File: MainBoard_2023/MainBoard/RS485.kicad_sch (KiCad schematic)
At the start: 18 parts

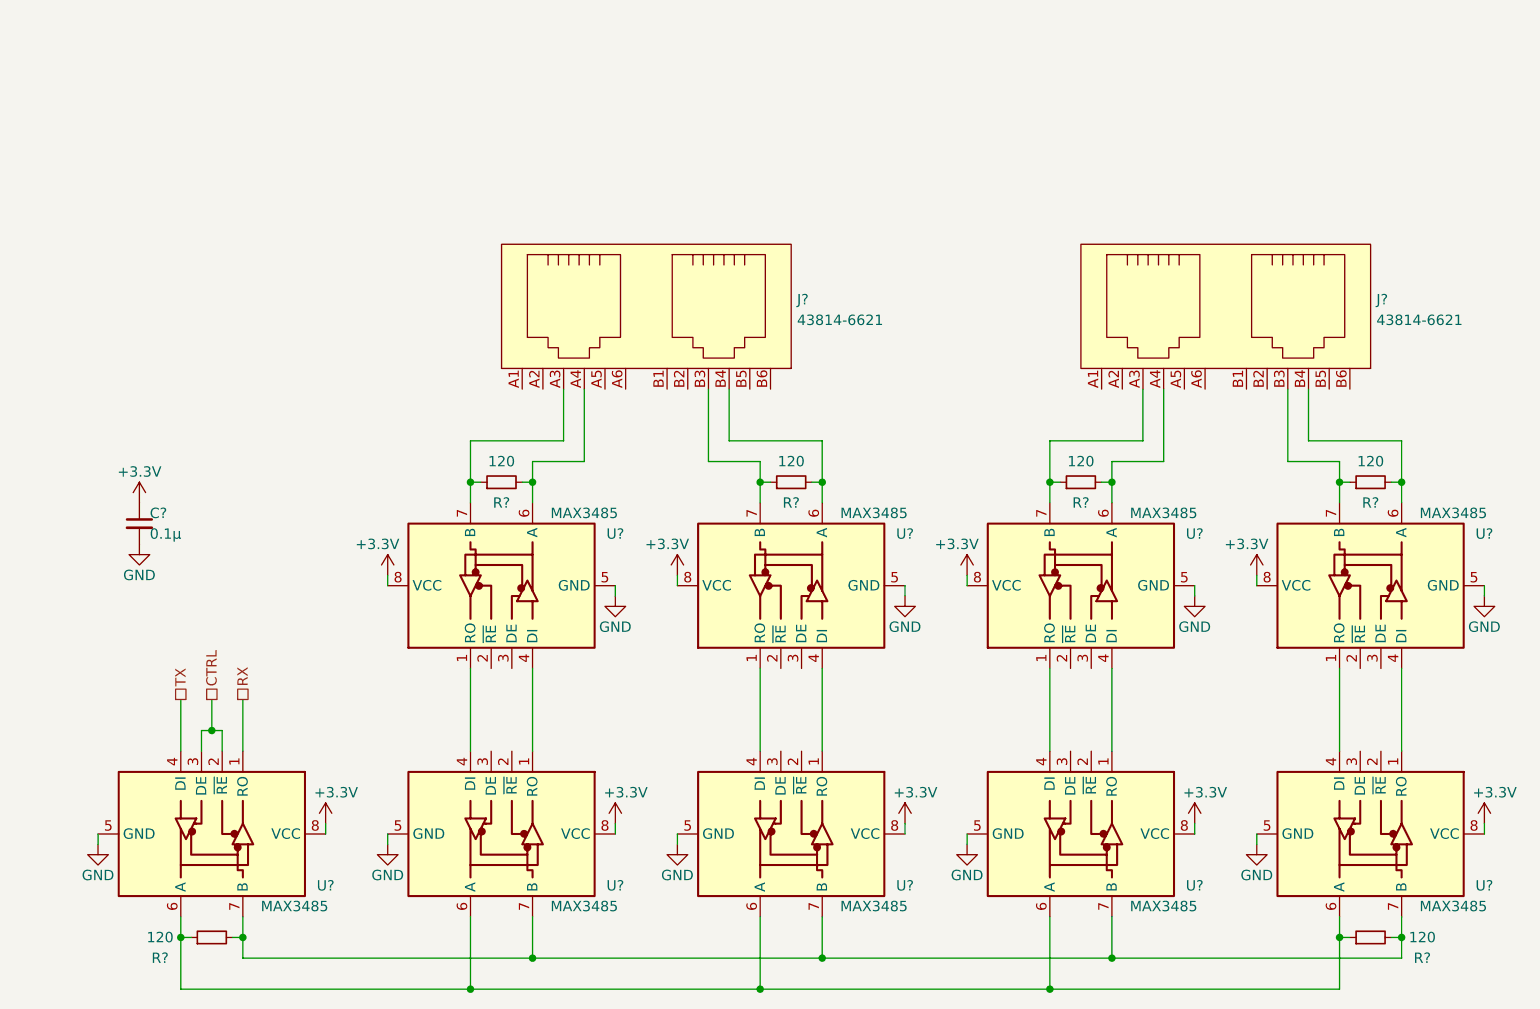
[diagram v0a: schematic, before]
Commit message: picoのピンを設定
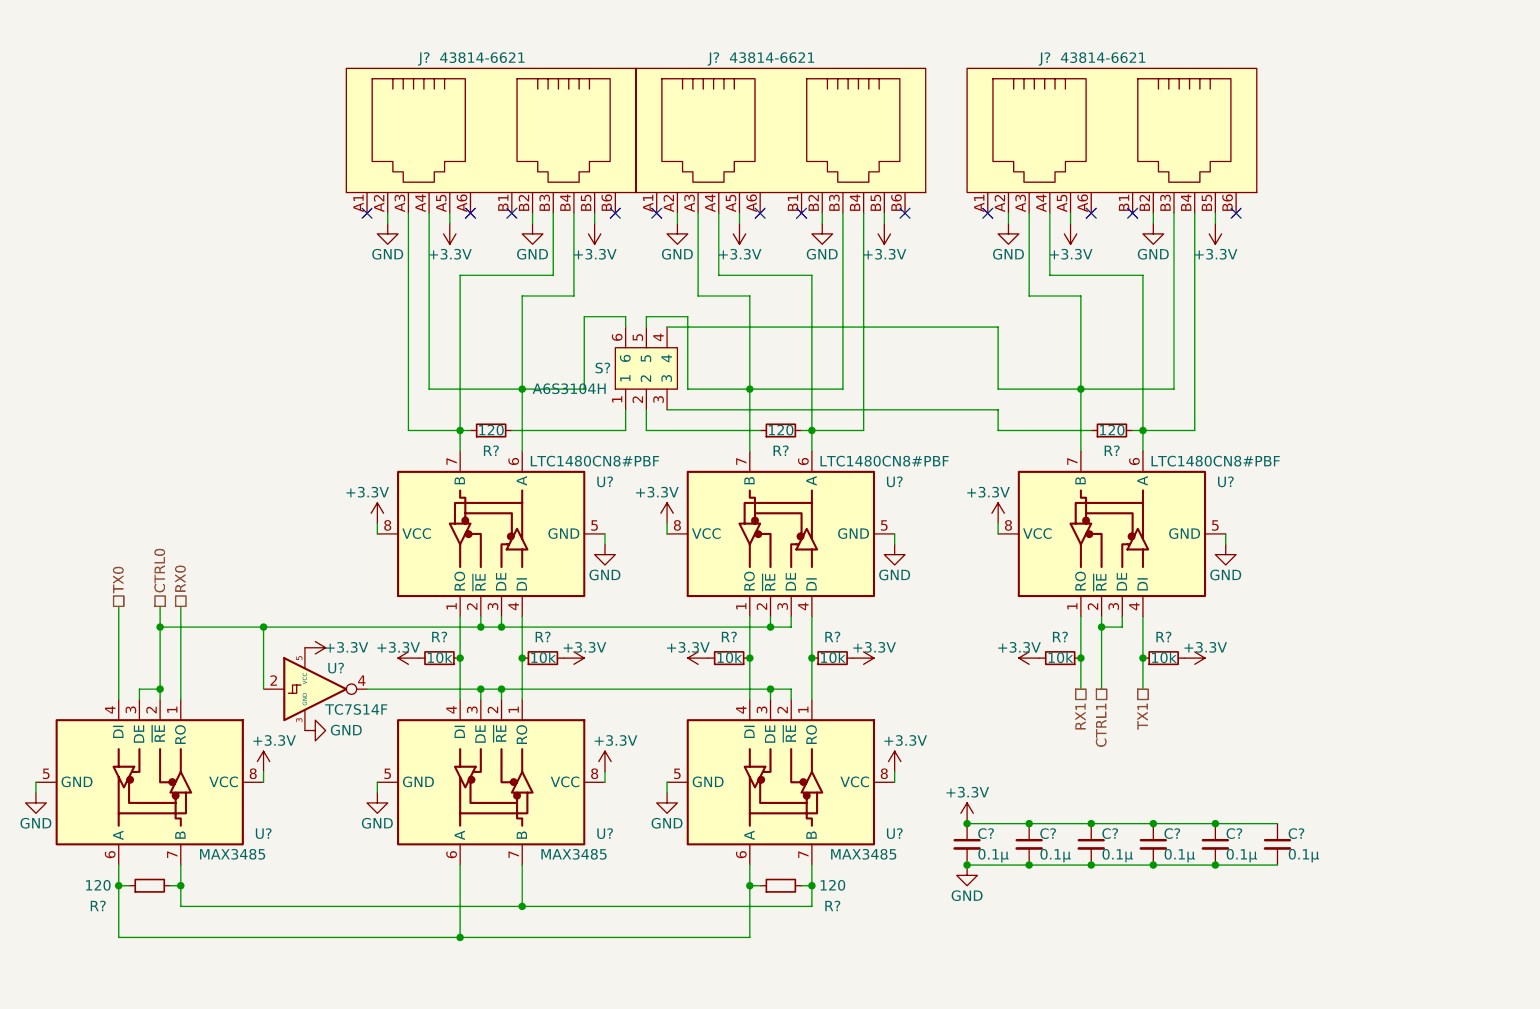
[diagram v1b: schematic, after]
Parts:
- removed J?: 43814-6621, 438146621, symbol Molex_6P6C_Right_Angle_TH_RJ11_Modular_Jack_Connector:43814-6621
- removed R? (x5): 120, symbol Device:R_Small
- removed U? (x6): MAX3485, symbol Interface_UART:MAX3485
- added C? (x5): 0.1μ, symbol Device:C_Small
- added J? (x2): 43814-6621, 438146621, symbol Molex_6P6C_Right_Angle_TH_RJ11_Modular_Jack_Connector:43814-6621
- added R? (x4): 120, symbol Device:R_Small
- added R? (x6): 10k, symbol Device:R_Small
- added S?: A6S3104H, SOP254P980X380-6N, symbol A6S-3104-H:A6S3104H
- added U? (x3): LTC1480CN8#PBF, symbol Interface_UART:MAX485E
- added U?: TC7S14F, Package_TO_SOT_SMD:SOT-23-5, symbol 74xGxx:SN74LVC1G14DBV
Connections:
- net +3.3V: now also J?.A5, J?.B5, C?.1, C?.1, C?.1, C?.1, C?.1, J?.A5, J?.A5, J?.B5, J?.B5, R?.2, R?.2, R?.2, R?.2, R?.2, R?.2, U?.5 (VCC), U?.8 (VCC), U?.8 (VCC), U?.8 (VCC)
- net GND: now also J?.A2, J?.B2, C?.2, C?.2, C?.2, C?.2, C?.2, J?.A2, J?.A2, J?.B2, J?.B2, U?.3 (GND), U?.5 (GND), U?.5 (GND), U?.5 (GND)
- net at U?.4 (DI): now also R?.1, U?.1 (RO) (x2)
- net at U?.1 (RO): now also R?.1, U?.4 (DI) (x2)
- net at J?.A4: now also J?.B4, S?.6, U?.6 (A)
- net at J?.A3: now also J?.B3, R?.1, U?.7 (B)
- net at R?.1, U?.6 (A), U?.6 (A)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: now also R?.1
- net at R?.2, U?.7 (B), U?.7 (B)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: now also R?.2
- net at U?.2 (~{RE}): now also U?.2 (~{RE}), U?.3 (DE), U?.3 (DE), U?.4
- net CTRL renamed CTRL0
- net CTRL0: now also U?.2, U?.2 (~{RE}), U?.2 (~{RE}), U?.3 (DE), U?.3 (DE)
- net RX renamed RX0
- net TX renamed TX0
- new net: R?.1, S?.2
- new net: J?.A4, J?.B4, R?.2, U?.6 (A) (x2)
- new net: R?.2, S?.1
- new net: J?.A3, J?.B3, S?.4, U?.7 (B)
- new net: R?.1, S?.3
- new net: J?.A3, J?.B3, S?.5, U?.7 (B)
- new net CTRL1: U?.2 (~{RE}), U?.3 (DE)
- new net RX1: R?.1, U?.1 (RO)
- new net TX1: R?.1, U?.4 (DI)
- no-connect marks 0 -> 12
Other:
- moved on the sheet: C?, J?, R?, U?

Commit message: ERC通った
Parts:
- gave numbers to parts that had none: 28

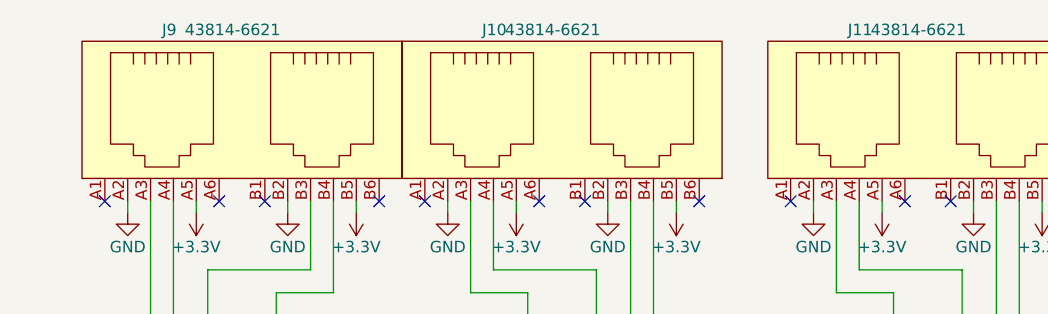
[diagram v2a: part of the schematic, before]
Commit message: フットプリントをすべて割り当て
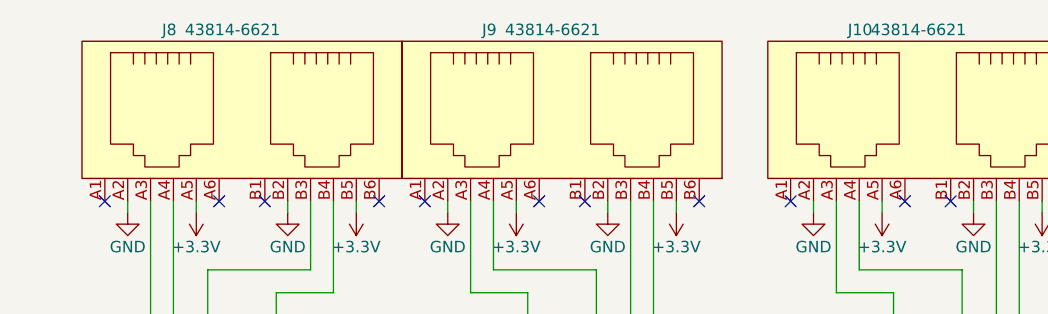
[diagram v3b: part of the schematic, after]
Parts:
- C18, C19, C20, C21, C22, C23: footprint (none) -> Capacitor_SMD:C_0603_1608Metric_Pad1.08x0.95mm_HandSolder
- J10: renamed from J11; footprint 438146621 -> Molex_6P6C_Right_Angle_TH_RJ11_Modular_Jack_Connector:Molex_6P6C_Right_Angle_TH_RJ11_Modular_Jack_Connector
- J8: renamed from J9; footprint 438146621 -> Molex_6P6C_Right_Angle_TH_RJ11_Modular_Jack_Connector:Molex_6P6C_Right_Angle_TH_RJ11_Modular_Jack_Connector
- J9: renamed from J10; footprint 438146621 -> Molex_6P6C_Right_Angle_TH_RJ11_Modular_Jack_Connector:Molex_6P6C_Right_Angle_TH_RJ11_Modular_Jack_Connector
- R31, R32, R33, R34, R35, R36, R37, R38, R39, R40, R41: footprint (none) -> Resistor_SMD:R_0603_1608Metric_Pad0.98x0.95mm_HandSolder
- S4: footprint SOP254P980X380-6N -> A6S-3104-H:A6S-3104-H
- U10, U12, U7: footprint (none) -> MAX3485ECSA:MAX3485ECSA
- U11, U13, U9: footprint (none) -> Package_DIP:DIP-8_W7.62mm_LongPads
- U8: footprint Package_TO_SOT_SMD:SOT-23-5 -> TC7S14F:TC7S14F

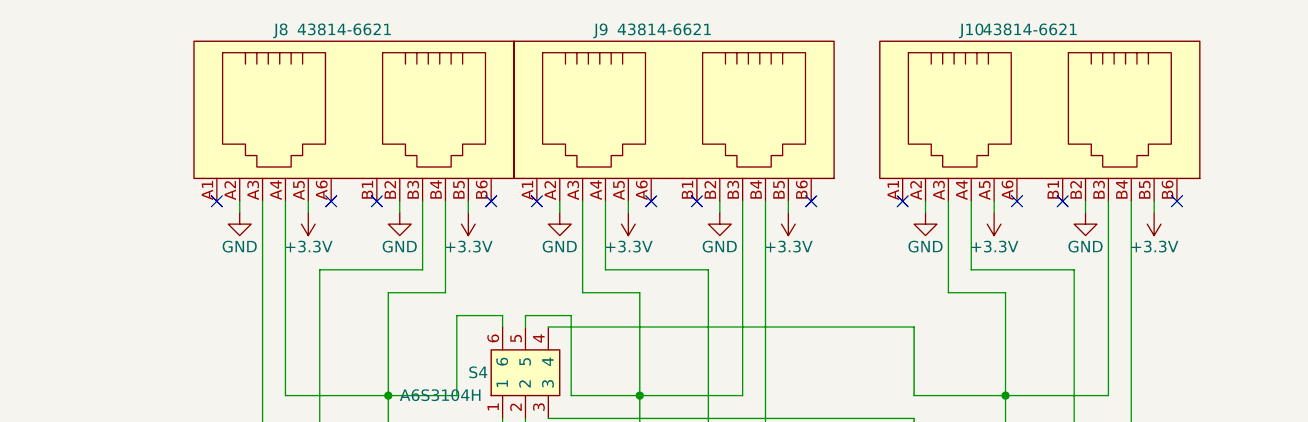
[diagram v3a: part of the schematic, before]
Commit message: 部品配置中　モジュラーコネクタを廃止
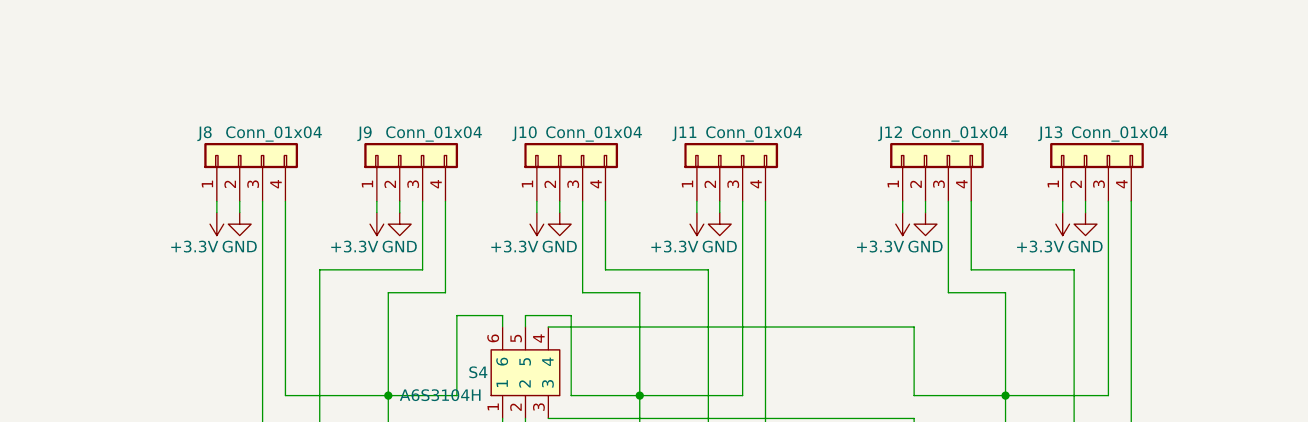
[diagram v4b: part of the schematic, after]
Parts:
- removed J10, J8, J9: 43814-6621, Molex_6P6C_Right_Angle_TH_RJ11_Modular_Jack_Connector:Molex_6P6C_Right_Angle_TH_RJ11_Modular_Jack_Connector, symbol Molex_6P6C_Right_Angle_TH_RJ11_Modular_Jack_Connector:43814-6621
- added J10, J11, J12, J13, J8, J9: Conn_01x04, symbol Connector_Generic:Conn_01x04
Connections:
- net +3.3V: now also J10.1 (Pin_1), J11.1 (Pin_1), J12.1 (Pin_1), J13.1 (Pin_1), J8.1 (Pin_1), J9.1 (Pin_1)
- net GND: now also J10.2 (Pin_2), J11.2 (Pin_2), J12.2 (Pin_2), J13.2 (Pin_2), J8.2 (Pin_2), J9.2 (Pin_2)
- net at R36.2, U11.6 (A): now also J10.4 (Pin_4), J11.4 (Pin_4)
- net at R33.1, U9.7 (B): now also J8.3 (Pin_3), J9.3 (Pin_3)
- net at S4.6, U9.6 (A): now also J8.4 (Pin_4), J9.4 (Pin_4)
- net at R40.2, U13.6 (A): now also J12.4 (Pin_4), J13.4 (Pin_4)
- net at S4.4, U13.7 (B): now also J12.3 (Pin_3), J13.3 (Pin_3)
- net at S4.5, U11.7 (B): now also J10.3 (Pin_3), J11.3 (Pin_3)
- no-connect marks 12 -> 0

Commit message: 部品配置中
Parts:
- J10, J11, J12, J13, J8, J9: footprint (none) -> Connector_JST:JST_XA_S04B-XASK-1_1x04_P2.50mm_Horizontal
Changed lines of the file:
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@@
     (property "Reference" "J10" (id 0) (at 138.43 49.53 90))
     (property "Value" "Conn_01x04" (id 1) (at 146.05 49.53 90))
-    (property "Footprint" "" (id 2) (at 142.24 52.07 0)
+    (property "Footprint" "Connector_JST:JST_XA_S04B-XASK-1_1x04_P2.50mm_Horizontal" (id 2) (at 142.24 52.07 0)
       (effects (font (size 1.27 1.27)) hide)
     )
@@
     (property "Reference" "J8" (id 0) (at 102.87 49.53 90))
     (property "Value" "Conn_01x04" (id 1) (at 110.49 49.53 90))
-    (property "Footprint" "" (id 2) (at 106.68 52.07 0)
+    (property "Footprint" "Connector_JST:JST_XA_S04B-XASK-1_1x04_P2.50mm_Horizontal" (id 2) (at 106.68 52.07 0)
       (effects (font (size 1.27 1.27)) hide)
     )
@@
     (property "Reference" "J12" (id 0) (at 179.07 49.53 90))
     (property "Value" "Conn_01x04" (id 1) (at 186.69 49.53 90))
-    (property "Footprint" "" (id 2) (at 182.88 52.07 0)
+    (property "Footprint" "Connector_JST:JST_XA_S04B-XASK-1_1x04_P2.50mm_Horizontal" (id 2) (at 182.88 52.07 0)
       (effects (font (size 1.27 1.27)) hide)
     )
@@
     (property "Reference" "J13" (id 0) (at 196.85 49.53 90))
     (property "Value" "Conn_01x04" (id 1) (at 204.47 49.53 90))
-    (property "Footprint" "" (id 2) (at 200.66 52.07 0)
+    (property "Footprint" "Connector_JST:JST_XA_S04B-XASK-1_1x04_P2.50mm_Horizontal" (id 2) (at 200.66 52.07 0)
       (effects (font (size 1.27 1.27)) hide)
     )
@@
     (property "Reference" "J9" (id 0) (at 120.65 49.53 90))
     (property "Value" "Conn_01x04" (id 1) (at 128.27 49.53 90))
-    (property "Footprint" "" (id 2) (at 124.46 52.07 0)
+    (property "Footprint" "Connector_JST:JST_XA_S04B-XASK-1_1x04_P2.50mm_Horizontal" (id 2) (at 124.46 52.07 0)
       (effects (font (size 1.27 1.27)) hide)
     )
@@
     (property "Reference" "J11" (id 0) (at 156.21 49.53 90))
     (property "Value" "Conn_01x04" (id 1) (at 163.83 49.53 90))
-    (property "Footprint" "" (id 2) (at 160.02 52.07 0)
-      (effects (font (size 1.27 1.27)) hide)
-    )
+    (property "Footprint" "Connector_JST:JST_XA_S04B-XASK-1_1x04_P2.50mm_Horizontal" (id 2) (at 160.02 52.07 0)
+      (effects (font (size 1.27 1.27)) hide)
+    )
